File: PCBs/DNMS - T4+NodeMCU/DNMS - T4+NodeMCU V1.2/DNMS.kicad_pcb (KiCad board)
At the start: 2 copper layers, 137.2 x 35.6 mm, 17 parts, among them J1 Conn_2Rows-07Pins, J2 Conn_01x02, J3 Conn_01x04, J4 Conn_01x05, U1 NodeMCU V2, U2 NodeMCU V3, U3 Teensy4.0

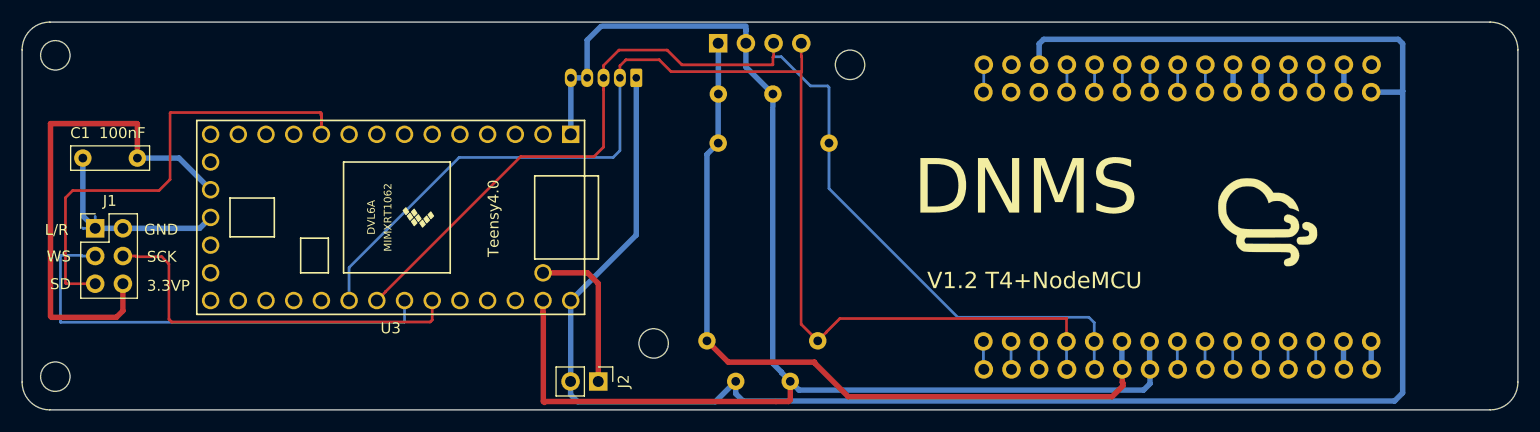
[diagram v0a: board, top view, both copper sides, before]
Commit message: change connector to mic to molex pico-ezmate
move other connectors around
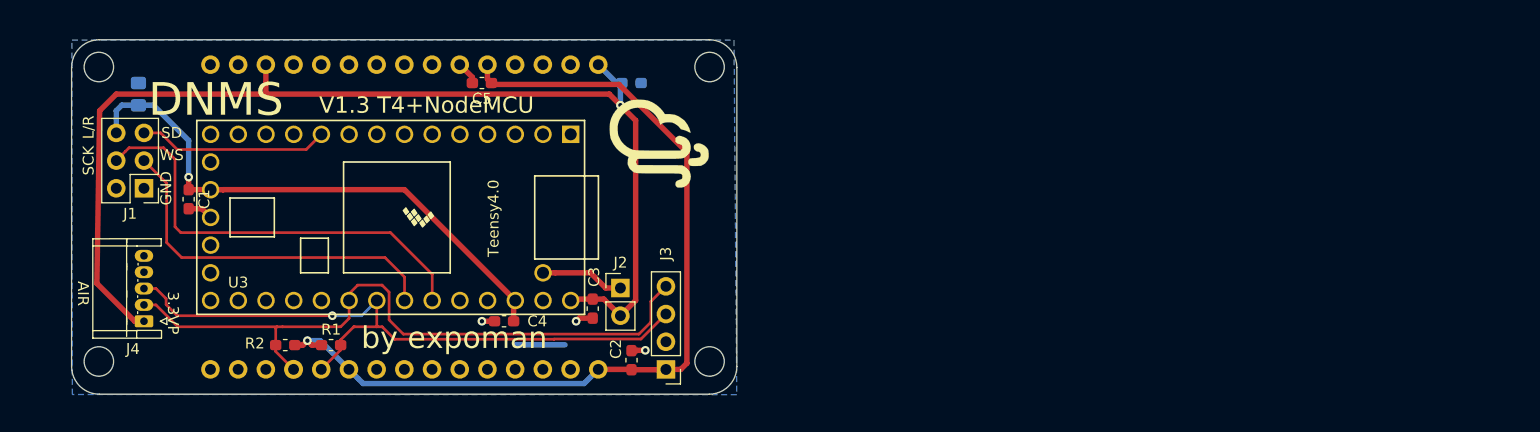
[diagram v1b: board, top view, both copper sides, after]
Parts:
- removed the REF1 at (136.9, 59.8)
- removed the REF1 at (118.9, 85.3)
- removed the REF1 at (64.0, 88.4)
- removed the REF1 at (64.0, 58.9)
- removed U1: NodeMCU V2, nodemcu:NodeMCU_Amica_R2
- added C4: 100nF, Capacitor_SMD:C_0603_1608Metric_Pad1.05x0.95mm_HandSolder, F.Cu at (105.2, 83.3)
- added C5: 100nF, Capacitor_SMD:C_0603_1608Metric_Pad1.05x0.95mm_HandSolder, F.Cu at (103.1, 61.5)
- added C6: 10uF, Capacitor_SMD:C_0805_2012Metric_Pad1.15x1.40mm_HandSolder, B.Cu at (71.6, 62.5)
- added C7: 100nF, Capacitor_SMD:C_0603_1608Metric_Pad1.05x0.95mm_HandSolder, B.Cu at (116.8, 61.5)
- added REF1: MountingHole_2.7mm_M2.5, MountingHole:MountingHole_2.7mm_M2.5, F.Cu at (124.0, 60.0)
- added REF1: MountingHole_2.7mm_M2.5, MountingHole:MountingHole_2.7mm_M2.5, F.Cu at (124.0, 87.0)
- added REF1: MountingHole_2.7mm_M2.5, MountingHole:MountingHole_2.7mm_M2.5, F.Cu at (68.0, 87.0)
- added REF1: MountingHole_2.7mm_M2.5, MountingHole:MountingHole_2.7mm_M2.5, F.Cu at (68.0, 60.0)
- C1: footprint Capacitor_THT:C_Rect_L7.0mm_W2.0mm_P5.00mm -> Capacitor_SMD:C_0603_1608Metric_Pad1.05x0.95mm_HandSolder
- C2, C3: footprint Capacitor_THT:C_Rect_L7.0mm_W2.0mm_P5.00mm -> Capacitor_SMD:C_0603_1608Metric_Pad1.05x0.95mm_HandSolder; moved to F.Cu
- J1: value Conn_2Rows-07Pins -> Conn_02x03_Odd_Even
- J3, J4: moved to F.Cu
- R1, R2: footprint Resistor_THT:R_Axial_DIN0207_L6.3mm_D2.5mm_P10.16mm_Horizontal -> Resistor_SMD:R_0603_1608Metric_Pad1.05x0.95mm_HandSolder; moved to F.Cu
- moved U2 70.9 mm to (98.6, 73.8)
- moved G*** 56.3 mm to (119.4, 67.1)
- moved J4 50.4 mm to (72.1, 83.3), turned to 90 degrees
- moved R1 40.0 mm to (89.3, 85.5)
- moved R2 38.7 mm to (85.1, 85.5), turned to 180 degrees
- moved J3 30.3 mm to (120.0, 87.7), turned to 180 degrees
- moved C2 25.7 mm to (116.8, 86.9), turned to 90 degrees
- moved C3 14.7 mm to (113.3, 82.2), turned to 270 degrees
- moved J2 8.81 mm to (115.8, 80.3), turned to 0 degrees
- moved C1 6.03 mm to (76.2, 72.1), turned to 270 degrees
- moved J1 5.78 mm to (72.1, 71.1), turned to 180 degrees
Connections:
- U2 pad 15: Net-(U2-Pad15) -> +5V
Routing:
- net GND: track 157.9 -> 13.2 mm, vias 0 -> 3
- net +5V: track 181.1 -> 103.8 mm, vias 0 -> 1
- net SDA: track 113.8 -> 62.5 mm
- net SCL: track 103.2 -> 61.3 mm, vias 0 -> 1
- net SD: track 43.6 -> 17.5 mm
- net WS: track 42.9 -> 33.6 mm
- net Net-(J2-Pad1): track 14.5 -> 7.68 mm
- net +3.3VP: track 46.1 -> 50.9 mm, vias 0 -> 1
- net SCK: track 35.7 -> 40.3 mm
- net +3V3: track 77.7 -> 82.0 mm, vias 0 -> 1
- net Net-(U2-Pad30): track 2.58 -> 0.00 mm
- net Net-(U2-Pad29): track 2.58 -> 0.00 mm
- net Net-(U2-Pad23): track 2.58 -> 0.00 mm
- net Net-(U2-Pad22): track 2.58 -> 0.00 mm
- net Net-(U2-Pad20): track 2.58 -> 0.00 mm
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- added copper zone on B.Cu, net GND
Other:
- board size 137.2 x 35.6 mm -> 61 x 32.5 mm
- board text added: "AIR"
- board text added: "V1.3 T4+NodeMCU"
- board text added: "by expoman"
- board text removed: "V1.2 T4+NodeMCU"
